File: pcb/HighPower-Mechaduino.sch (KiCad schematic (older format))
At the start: 49 parts, among them J1 SUPPLY, J2 STEPPER, P1 SWD, P4 -, P5 -, P6 -, P7 -, Q1 SSM3J328R, Q2 BSS138, SW1 SW_PUSH, U1 AS5047D, U2 AP2112K-3.3TRG1, U3 AT24CS64-SSHM

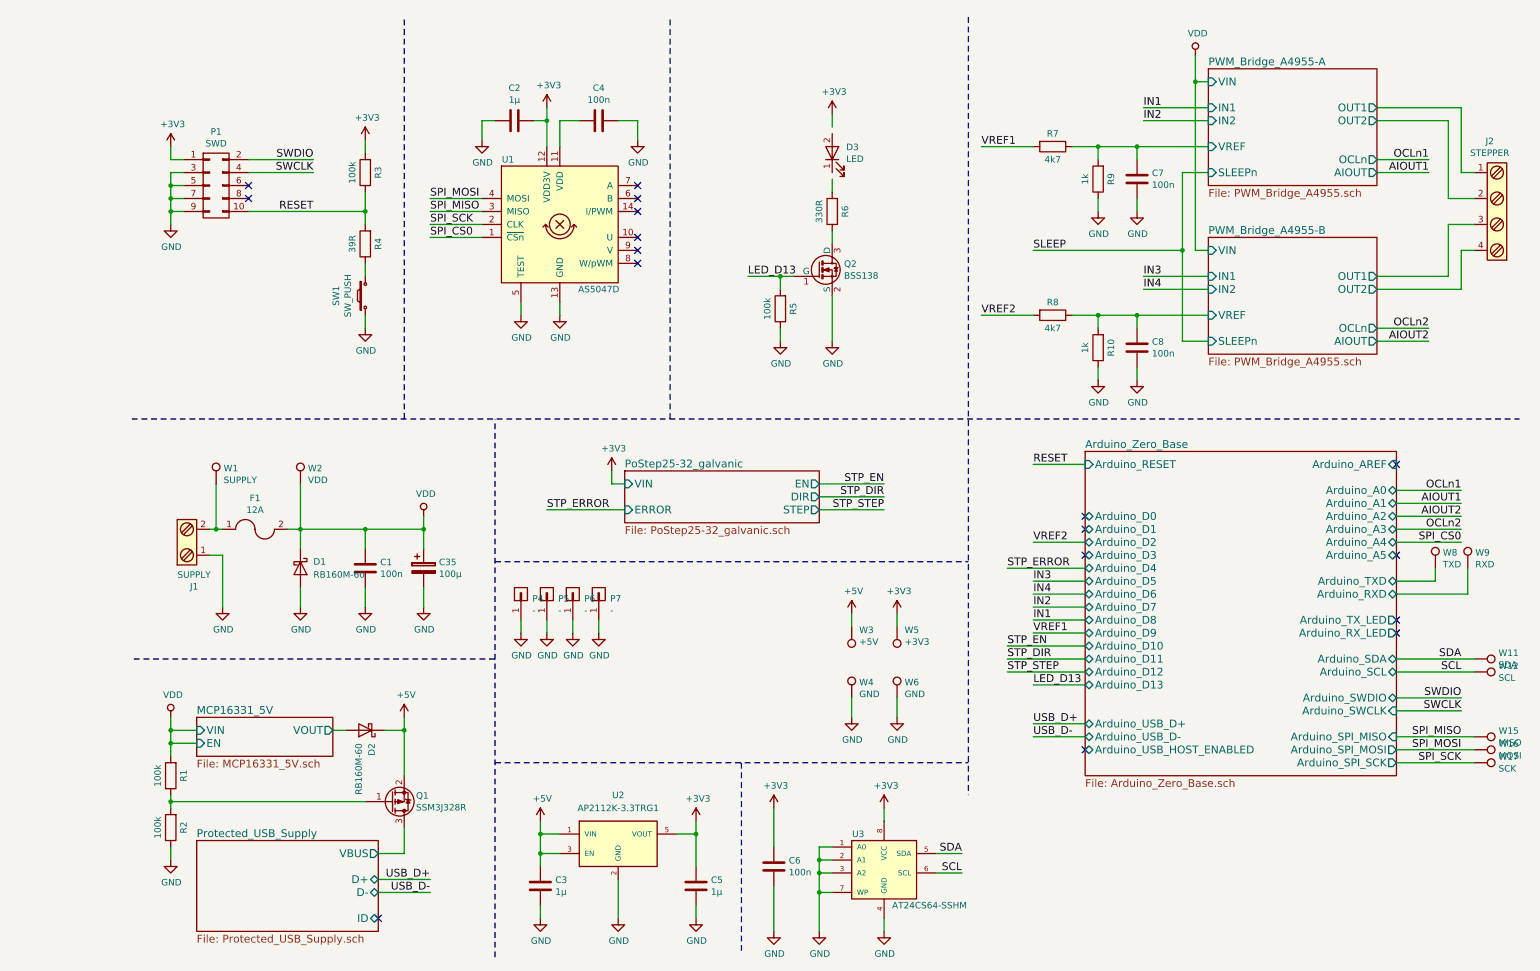
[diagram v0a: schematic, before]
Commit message: Add some little changes to the schematic, add calculations
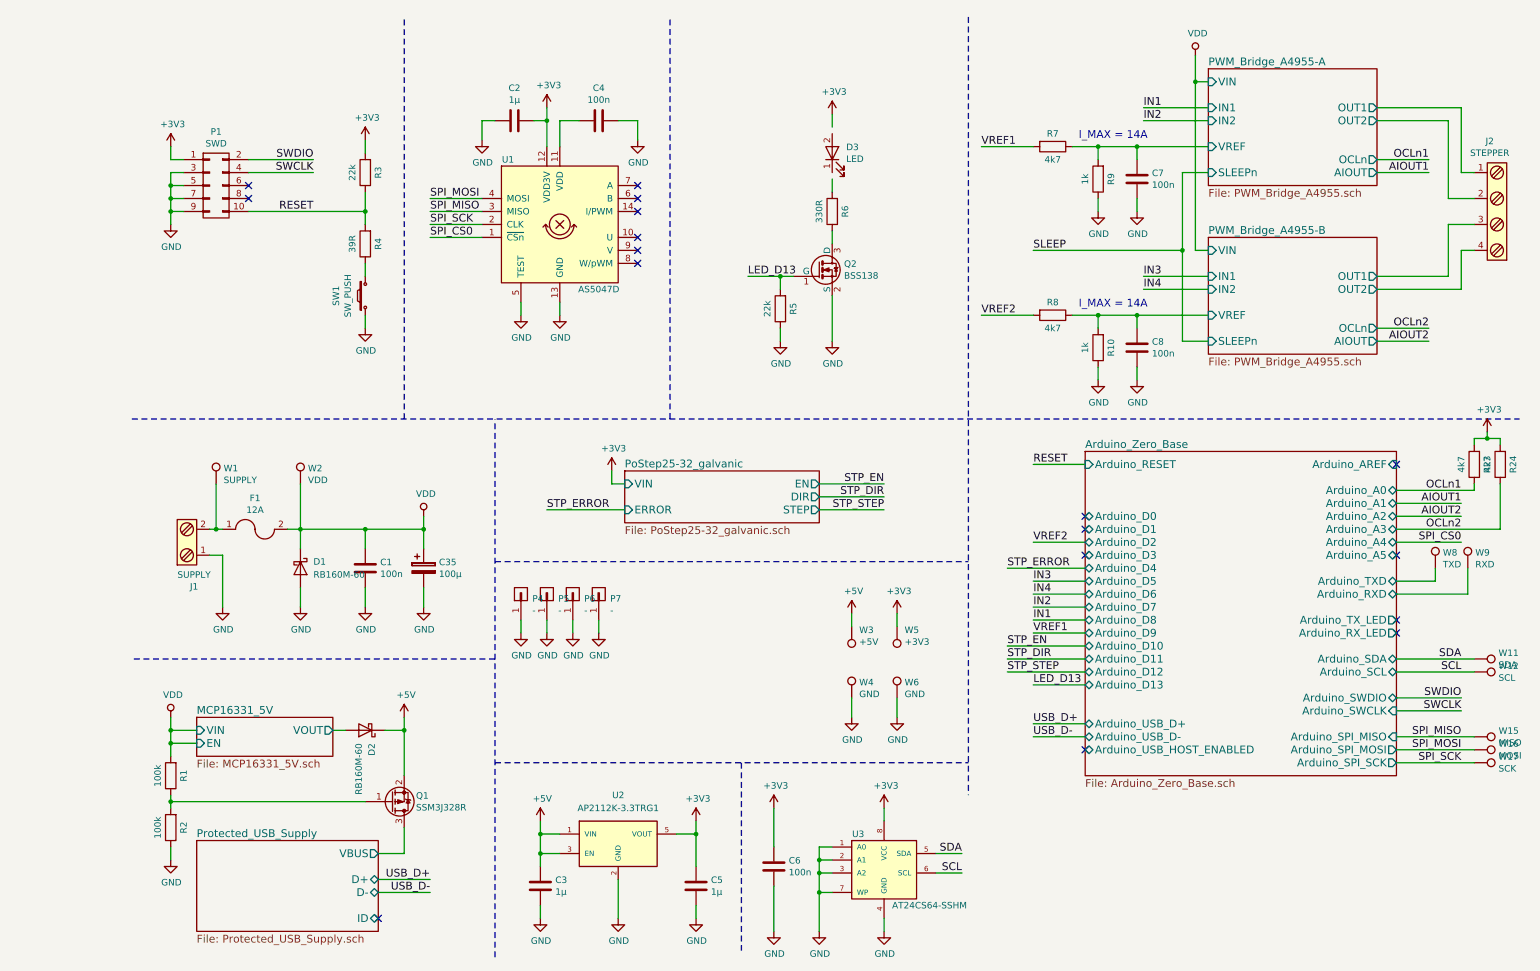
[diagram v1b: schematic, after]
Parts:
- added R23, R24: 4k7, Resistors_SMD:R_0603, symbol R
- R3, R5: value 100k -> 22k
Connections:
- net +3V3: now also R23.2, R24.2
- net OCLn1: now also R23.1
- net OCLn2: now also R24.1
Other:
- note added: "I_MAX = 14A"

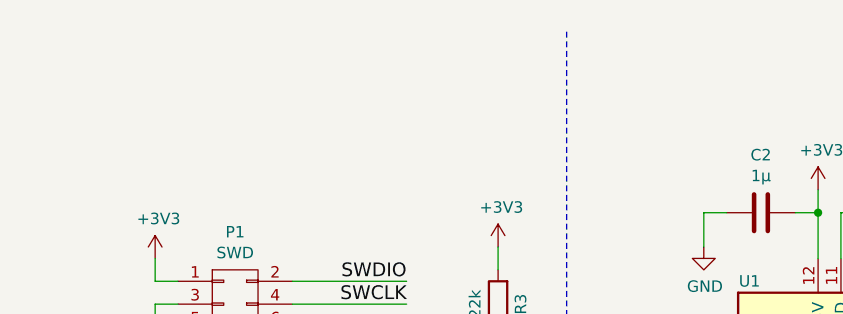
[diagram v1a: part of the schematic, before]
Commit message: Add some digikey order informations to components
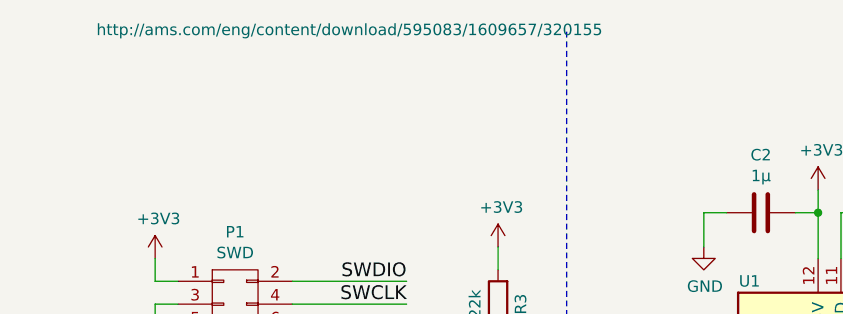
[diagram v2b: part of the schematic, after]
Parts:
- F1: Digi-Key Minimum Quantity (none) -> 1; Digi-Key Part Number (none) -> 507-2059-6-ND
- SW1: Digi-Key Minimum Quantity (none) -> 1; Digi-Key Part Number (none) -> SW1020CT-ND
- U1: Digi-Key Minimum Quantity (none) -> 1; Digi-Key Part Number (none) -> AS5047D-ATSMCT-ND
- U2: Digi-Key Minimum Quantity (none) -> 1; Digi-Key Part Number (none) -> AP2112K-3.3TRG1DICT-ND
- U3: Digi-Key Minimum Quantity (none) -> 1; Digi-Key Part Number (none) -> AT24CS64-SSHM-TCT-ND
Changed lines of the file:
@@
 F 1 "AS5047D" H 4100 1600 50  0000 C CNN
 F 2 "Housings_SSOP:TSSOP-14_4.4x5mm_Pitch0.65mm" H 3800 1350 50  0001 C CNN
-F 3 "" H 1650 3700 50  0000 C CNN
+F 3 "http://ams.com/eng/content/download/595083/1609657/320155" H 1650 3700 50  0000 C CNN
+F 4 "AS5047D-ATSMCT-ND" H 3800 2100 60  0001 C CNN "Digi-Key Part Number"
+F 5 "1" H 3800 2100 60  0001 C CNN "Digi-Key Minimum Quantity"
 	1    3800 2100
 	1    0    0    -1
@@
 F 1 "12A" H 1450 4599 50  0000 C CNN
 F 2 "Fuse_Holders_and_Fuses_local:Fuse_0679H" H 1450 4450 50  0001 C CNN
-F 3 "" H 1450 4450 50  0000 C CNN
+F 3 "http://belfuse.com/pdfs/0679H.pdf" H 1450 4450 50  0001 C CNN
+F 4 "507-2059-6-ND" H 1450 4450 60  0001 C CNN "Digi-Key Part Number"
+F 5 "1" H 1450 4450 60  0001 C CNN "Digi-Key Minimum Quantity"
 	1    1450 4450
 	1    0    0    -1
@@
 F 1 "AP2112K-3.3TRG1" H 4250 7100 50  0000 C CNN
 F 2 "TO_SOT_Packages_SMD:SOT-23-5" H 4250 7076 50  0001 C CIN
-F 3 "" H 4250 6850 50  0000 C CNN
+F 3 "http://www.diodes.com/_files/datasheets/AP2112.pdf" H 4250 6850 50  0001 C CNN
+F 4 "AP2112K-3.3TRG1DICT-ND" H 4250 6850 60  0001 C CNN "Digi-Key Part Number"
+F 5 "1" H 4250 6850 60  0001 C CNN "Digi-Key Minimum Quantity"
 	1    4250 6850
 	1    0    0    -1
@@
 F 1 "SW_PUSH" H 2300 2784 50  0000 C CNN
 F 2 "Buttons_Switches_SMD:SW_SPST_B3U-1000P" H 2300 2850 50  0001 C CNN
-F 3 "" H 2300 2850 50  0000 C CNN
+F 3 "http://www.omron.com/ecb/products/pdf/en-b3u.pdf" H 2300 2850 50  0001 C CNN
+F 4 "SW1020CT-ND" H 2300 2650 60  0001 C CNN "Digi-Key Part Number"
+F 5 "1" H 2300 2650 60  0001 C CNN "Digi-Key Minimum Quantity"
 	1    2300 2650
 	0    -1   -1   0
@@
 F 1 "AT24CS64-SSHM" H 6650 6750 50  0000 C CNN
 F 2 "Housings_SOIC:SOIC-8_3.9x4.9mm_Pitch1.27mm" H 6300 7050 50  0001 C CIN
-F 3 "" H 6300 7050 50  0000 C CNN
+F 3 "http://www.atmel.com/Images/Atmel-8861-SEEPROM-Atmel-Value-Added-Serial-EEPROM-Products-AT24MAC-AT24CS-Brochure.pdf" H 6300 7050 50  0001 C CNN
+F 4 "AT24CS64-SSHM-TCT-ND" H 6300 7050 60  0001 C CNN "Digi-Key Part Number"
+F 5 "1" H 6300 7050 60  0001 C CNN "Digi-Key Minimum Quantity"
 	1    6300 7050
 	1    0    0    -1

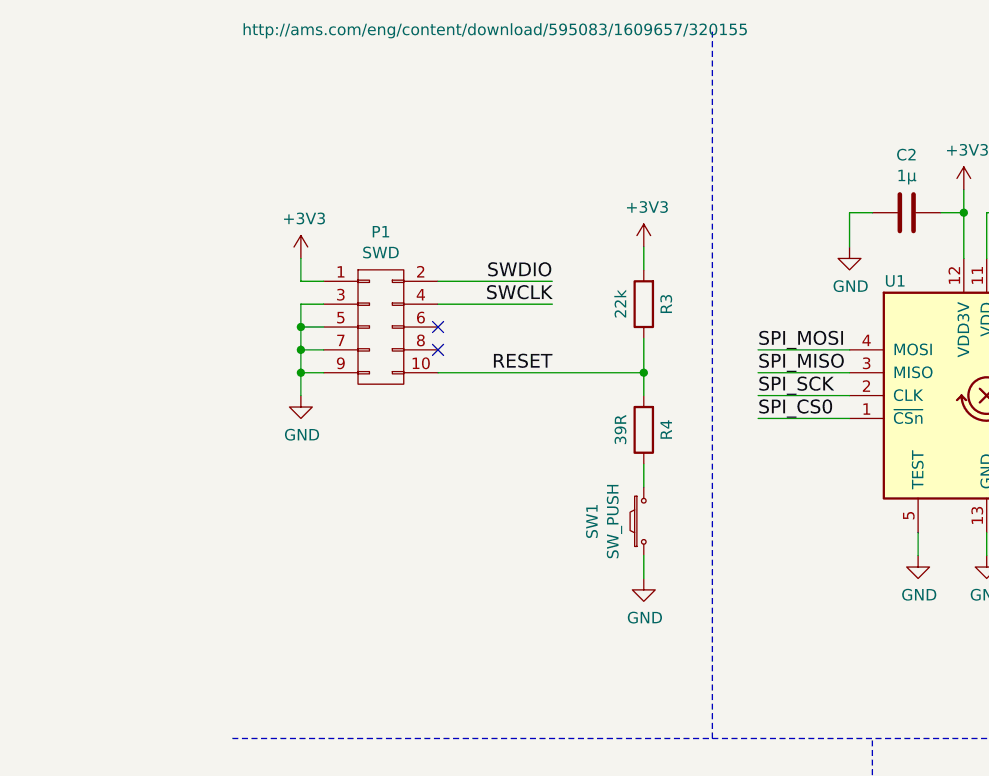
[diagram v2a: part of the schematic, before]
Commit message: Add more order informations, create BOM
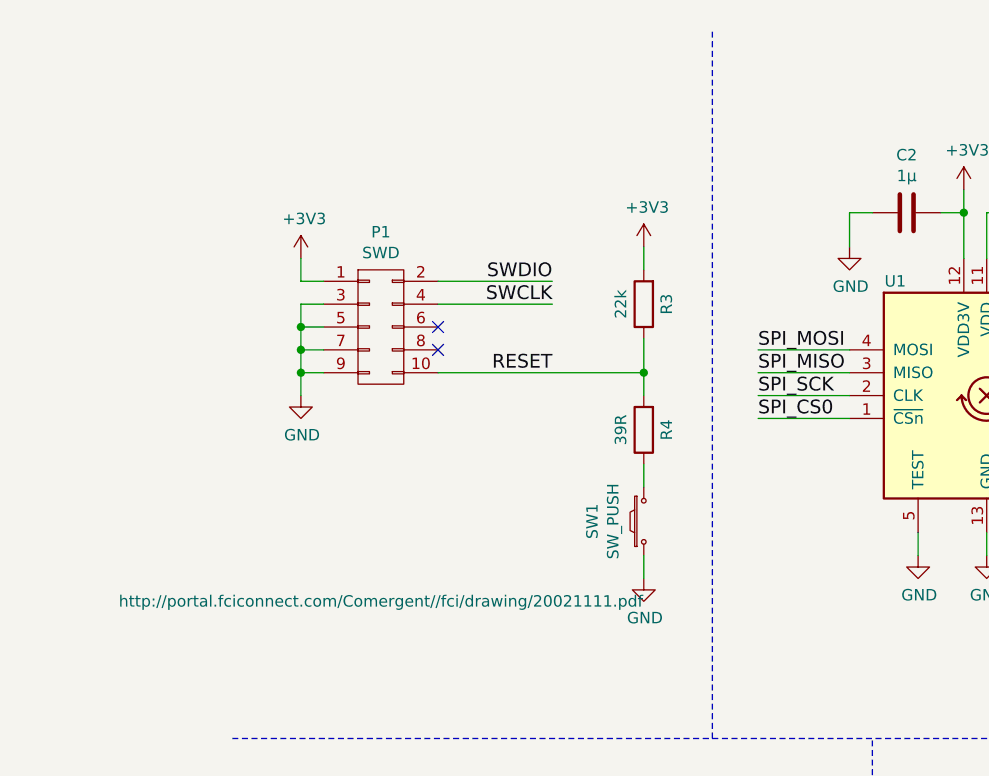
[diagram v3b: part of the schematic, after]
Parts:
- D1, D2: Digi-Key Minimum Quantity (none) -> 1; Digi-Key Part Number (none) -> RB160M-90DKR-ND
- P1: Digi-Key Minimum Quantity (none) -> 1; Digi-Key Part Number (none) -> 609-3712-ND
- Q1: Digi-Key Minimum Quantity (none) -> 1; Digi-Key Part Number (none) -> SSM3J328RLFCT-ND
- Q2: Digi-Key Minimum Quantity (none) -> 1; Digi-Key Part Number (none) -> BSS138NH6327XTSA2CT-ND
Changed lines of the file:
@@
 F 1 "AS5047D" H 4100 1600 50  0000 C CNN
 F 2 "Housings_SSOP:TSSOP-14_4.4x5mm_Pitch0.65mm" H 3800 1350 50  0001 C CNN
-F 3 "http://ams.com/eng/content/download/595083/1609657/320155" H 1650 3700 50  0000 C CNN
+F 3 "http://ams.com/eng/content/download/595083/1609657/320155" H 1650 3700 50  0001 C CNN
 F 4 "AS5047D-ATSMCT-ND" H 3800 2100 60  0001 C CNN "Digi-Key Part Number"
 F 5 "1" H 3800 2100 60  0001 C CNN "Digi-Key Minimum Quantity"
@@
 F 1 "SWD" H 1150 2124 50  0000 C CNN
 F 2 "Pin_Headers:Pin_Header_Straight_2x05_Pitch1.27mm" H 1150 600 50  0001 C CNN
-F 3 "" H 1150 600 50  0000 C CNN
+F 3 "http://portal.fciconnect.com/Comergent//fci/drawing/20021111.pdf" H 1150 600 50  0000 C CNN
+F 4 "609-3712-ND" H 1150 1800 60  0001 C CNN "Digi-Key Part Number"
+F 5 "1" H 1150 1800 60  0001 C CNN "Digi-Key Minimum Quantity"
 	1    1150 1800
 	1    0    0    -1
@@
 F 1 "BSS138" H 5991 2405 50  0000 L CNN
 F 2 "TO_SOT_Packages_SMD:SOT-23" H 6000 2375 50  0001 L CIN
-F 3 "" H 5800 2450 50  0000 L CNN
+F 3 "http://www.infineon.com/dgdl/Infineon-BSS138N-DS-v02_86-en.pdf?fileId=db3a304330f68606013104d944d53efb" H 5800 2450 50  0001 L CNN
+F 4 "BSS138NH6327XTSA2CT-ND" H 5800 2450 60  0001 C CNN "Digi-Key Part Number"
+F 5 "1" H 5800 2450 60  0001 C CNN "Digi-Key Minimum Quantity"
 	1    5800 2450
 	1    0    0    -1
@@
 F 1 "RB160M-60" V 2350 6100 50  0000 L CNN
 F 2 "Diodes_SMD:SOD-123" H 2300 6000 50  0001 C CNN
-F 3 "" H 2300 6000 50  0000 C CNN
+F 3 "http://rohmfs.rohm.com/en/products/databook/datasheet/discrete/diode/schottky_barrier/rb160m-60.pdf" H 2300 6000 50  0001 C CNN
+F 4 "RB160M-90DKR-ND" H 2300 6000 60  0001 C CNN "Digi-Key Part Number"
+F 5 "1" H 2300 6000 60  0001 C CNN "Digi-Key Minimum Quantity"
 	1    2300 6000
 	-1   0    0    1
@@
 F 1 "RB160M-60" V 1850 4850 50  0000 L CNN
 F 2 "Diodes_SMD:SOD-123" H 1800 4750 50  0001 C CNN
-F 3 "" H 1800 4750 50  0000 C CNN
+F 3 "http://rohmfs.rohm.com/en/products/databook/datasheet/discrete/diode/schottky_barrier/rb160m-60.pdf" H 1800 4750 50  0001 C CNN
+F 4 "RB160M-90DKR-ND" H 1800 4750 60  0001 C CNN "Digi-Key Part Number"
+F 5 "1" H 1800 4750 60  0001 C CNN "Digi-Key Minimum Quantity"
 	1    1800 4750
 	0    1    1    0
@@
 F 1 "SSM3J328R" H 2691 6595 50  0000 L CNN
 F 2 "TO_SOT_Packages_SMD:SOT-23" H 2700 6650 50  0001 C CNN
-F 3 "" H 2500 6550 50  0000 C CNN
+F 3 "https://toshiba.semicon-storage.com/info/docget.jsp?did=2429&prodName=SSM3J328R" H 2500 6550 50  0001 C CNN
+F 4 "SSM3J328RLFCT-ND" H 2500 6550 60  0001 C CNN "Digi-Key Part Number"
+F 5 "1" H 2500 6550 60  0001 C CNN "Digi-Key Minimum Quantity"
 	1    2500 6550
 	1    0    0    1
